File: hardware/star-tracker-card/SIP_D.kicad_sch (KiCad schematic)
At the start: 5 parts, among them J6 Conn_01x02, U7 OSD3358-512M-BSM

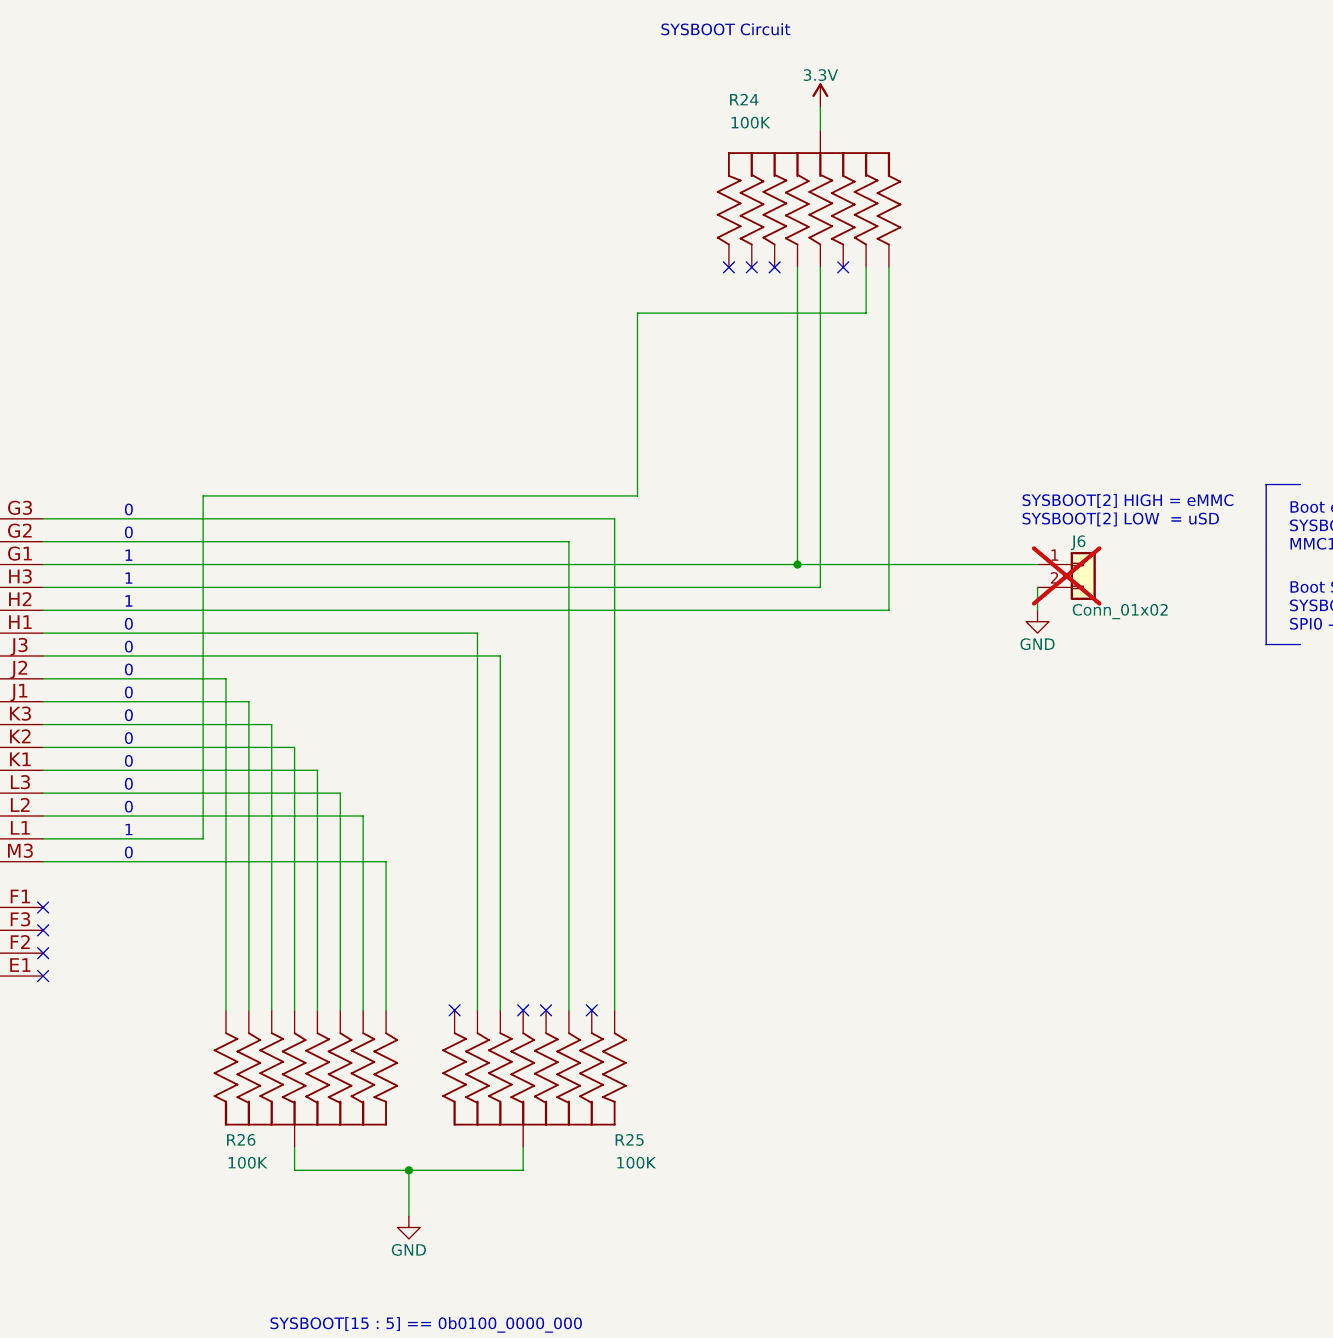
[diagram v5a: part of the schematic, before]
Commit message: Star Tracker v1.3 files, including new Makefile, Readme, and fixes in ERC, DRC, and layout
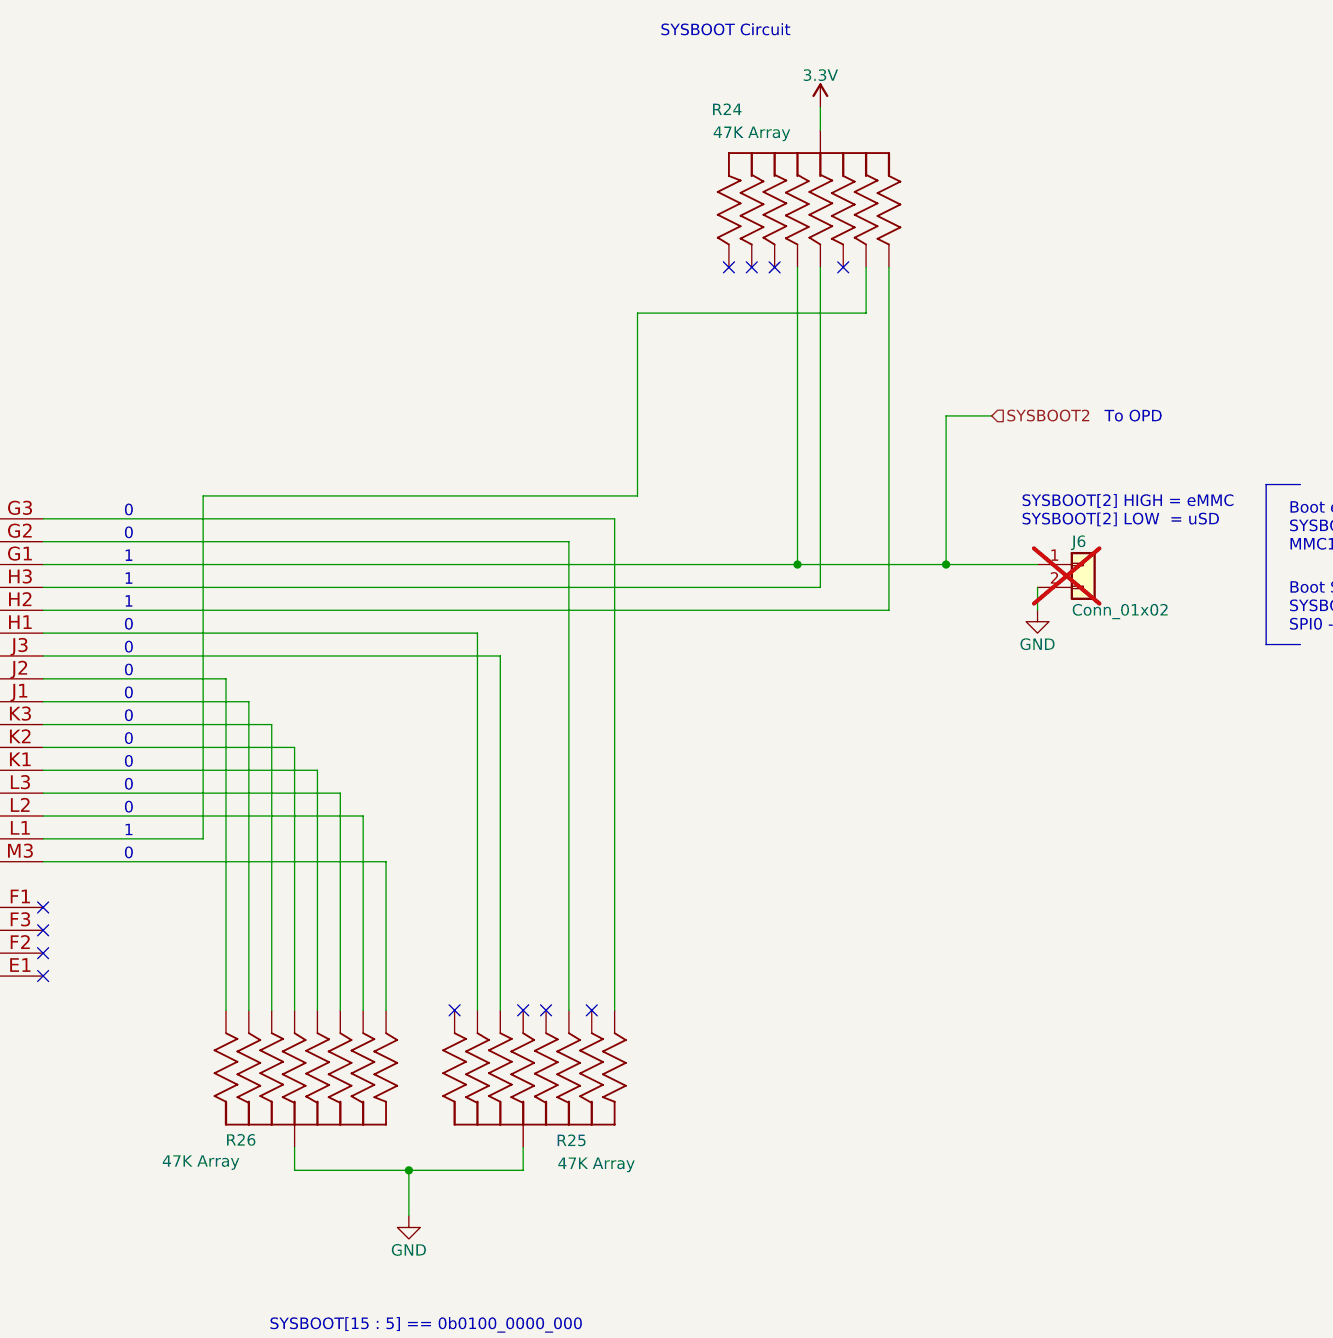
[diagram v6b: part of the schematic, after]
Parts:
- R24, R25, R26: value 100K -> 47K Array; DPN U7104CT-ND -> U7473CT-ND; MFR Panasonic Industry -> Panasonic Electronic Components; MPN EXB-A10P104J -> EXB-A10P473J
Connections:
- net SYSBOOT2: now reaches J6.1 (Pin_1), R24.8 (88), U7.G1 (LCD_DATA2)
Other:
- note added: "To OPD"
